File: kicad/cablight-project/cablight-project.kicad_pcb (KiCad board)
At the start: 4 copper layers, 72 x 40 mm, 62 parts, among them J3 Screw_Term_1x4_5mm, M2.5 MountingHole_2.7mm_M2.5_ISO73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, Q1 IRLB8721PBF, SW1 switch_SPDT_SLW_121586, T1 ISL85410, U1 TPD2EUSB30, U3 ESP32-S3-WROOM-1U

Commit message: further board changes
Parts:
- B1: renamed from RESET1; value Tactile -> RESET - TACTILE SMD
- B2: renamed from BOOT1; value tactile -> BOOT - TACTILE SMD
- C5: value 10uF -> 22uF
- LED1: renamed from LED-W1; value LED -> LED 0603
- LED2: renamed from LED-OK1; value LED -> LED 0603
- SW1: value switch_SPDT_SLW_121586 -> SHUNT JUMPER
- moved C4 13.8 mm to (78.3, 50.6), turned to -90 degrees
- moved R1 3.26 mm to (94.2, 46.5)
- moved R3 1.10 mm to (92.9, 70.0)
- moved R10 0.80 mm to (72.5, 44.9)
- moved M2.5 0.47 mm to (63.4, 46.5)
- moved CP4 0.45 mm to (83.8, 59.7)
- moved CP5 0.45 mm to (81.5, 59.7)
- moved CP6 0.45 mm to (79.2, 59.7)
- moved D3 0.40 mm to (113.7, 46.1)
- moved TP2 0.32 mm to (109.6, 47.1)
- moved C9 0.31 mm to (67.7, 45.8)
- moved R11 0.30 mm to (67.7, 49.9)
- moved C6 0.30 mm to (92.9, 66.3)
- moved C8 0.30 mm to (112.6, 53.6)
- moved M2.5 0.30 mm to (122.7, 72.4)
- renumbered D10 to D2, D2 to D3, J3 to J1, RCWL-1601 to J2, USBC-V1 to USBC1
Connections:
- net 3.3V renamed 3V3
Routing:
- net PG: track 41.8 -> 44.0 mm
- net 3V3: track 97.7 -> 96.2 mm
- net /VBUS: track 22.6 -> 23.3 mm
- net ECHO: vias 3 -> 1
- net GND: vias 67 -> 77
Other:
- board size 72 x 40 mm -> 72.7 x 40 mm
- board text added: "Ultrasonic LED Controller Designed by George R. Kuegler v4.0 - 2025-12-02 Haverhill, MA github.com/gkuegler"
- board text added: "move this back measure with a caliper button from pin layout"
- board text removed: "Ultrasonic Lighting Controller Designed by George R. Kuegler v4.0 - 2025-11-24 Haverhill, MA github.com/gkuegler"
- board text removed: "move this back"

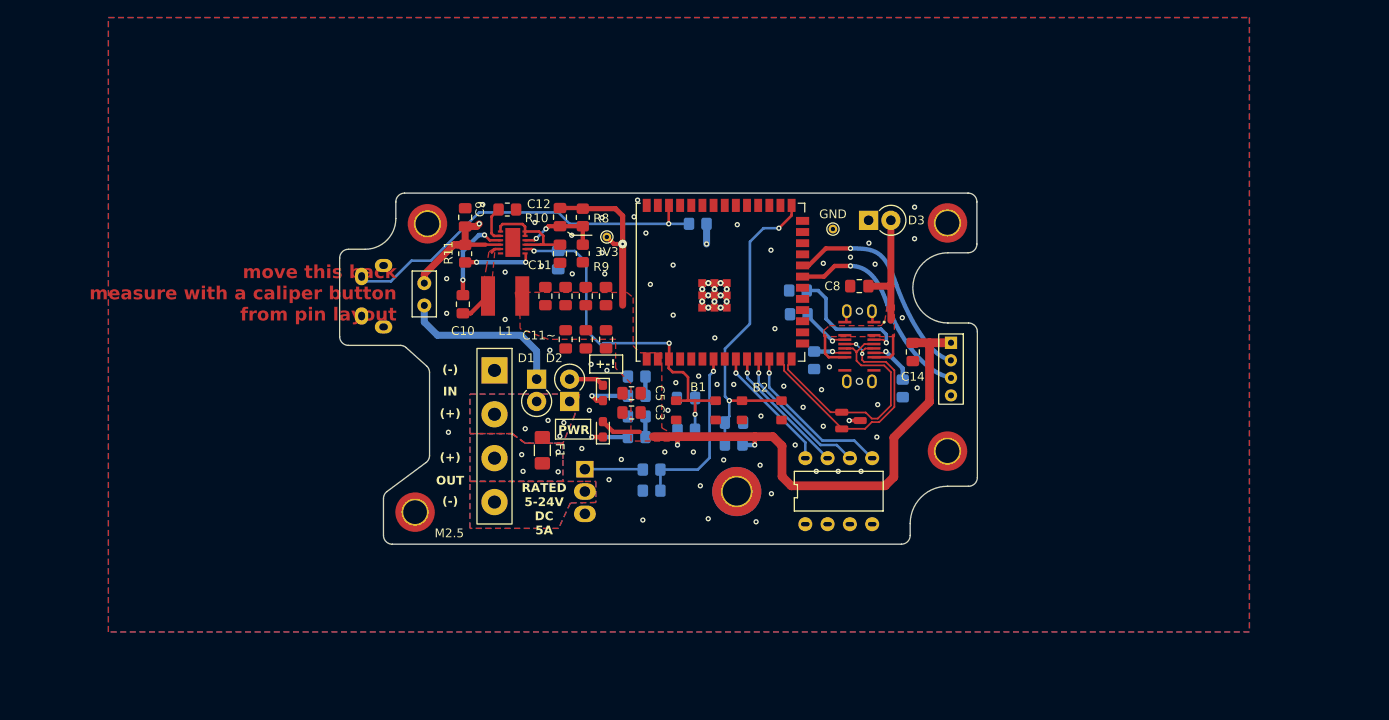
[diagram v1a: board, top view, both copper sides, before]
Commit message: add gate driver and linear regulator
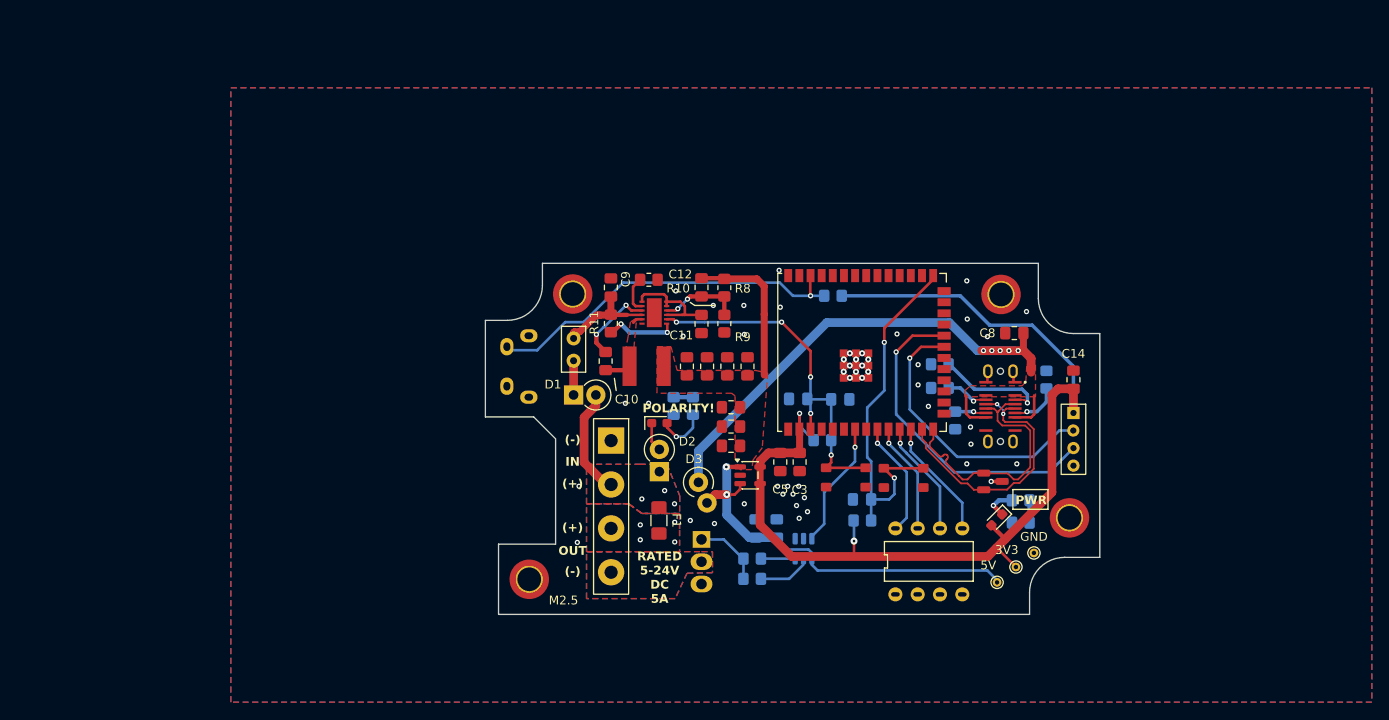
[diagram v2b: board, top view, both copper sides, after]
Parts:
- removed R4: 10K, Resistor_SMD:R_0805_2012Metric_Pad1.20x1.40mm_HandSolder
- removed REF**: MountingHole_3.2mm_M3_DIN965_Pad_TopBottom, MountingHole:MountingHole_3.2mm_M3_DIN965_Pad_TopBottom
- added C1: 2uF, Capacitor_SMD:C_0805_2012Metric_Pad1.18x1.45mm_HandSolder, B.Cu at (100.8, 81.2)
- added C2: 100nF, Capacitor_SMD:C_0805_2012Metric_Pad1.18x1.45mm_HandSolder, B.Cu at (103.2, 81.2)
- added R18: 0R, Resistor_SMD:R_0805_2012Metric_Pad1.20x1.40mm_HandSolder, B.Cu at (100.4, 84.7)
- added TP3: 5V, TestPoint:TestPoint_THTPad_D1.0mm_Drill0.5mm, F.Cu at (128.3, 87.3)
- added U2: 1EDN7550B, Package_TO_SOT_SMD:SOT-23-6, B.Cu at (106.2, 83.5)
- added U5: TLV73333PDBV, Package_TO_SOT_SMD:SOT-23-5, F.Cu at (100.2, 75.2)
- D3: value 1N5819 -> 1N5817
- R5: value 47R -> 5R
- R8: value 100K -> 91K
- R9: value 22K1 -> 12K4
- moved TP2 59.9 mm to (130.4, 85.6)
- moved LED2 46.0 mm to (128.3, 80.2), turned to -135 degrees
- moved R17 45.4 mm to (131.0, 80.5)
- moved R14 44.3 mm to (131.0, 78.0)
- moved TP1 43.4 mm to (132.5, 84.0)
- moved D3 37.1 mm to (95.2, 78.3), turned to 112.5 degrees
- moved C4 31.6 mm to (105.6, 66.5), turned to 180 degrees
- moved CP6 20.4 mm to (98.0, 67.4), turned to 180 degrees
- moved C3 20.0 mm to (105.8, 73.6), turned to -90 degrees
- moved CP5 19.3 mm to (98.0, 69.6), turned to 180 degrees
- moved B1 18.7 mm to (113.3, 76.5)
- moved CP4 18.7 mm to (98.0, 71.8), turned to 180 degrees
- moved C5 18.7 mm to (103.6, 73.6), turned to -90 degrees
- moved C14 18.6 mm to (137.0, 64.3), turned to 90 degrees
- moved C8 18.5 mm to (130.3, 59.0)
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- renumbered TP2 to TP1, TP1 to TP2
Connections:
- C12 pad 1: 3V3 -> 5V
- C9 pad 1: 5V -> Net-(SW1-B)
- CP1 pad 1: 3V3 -> 5V
- CP2 pad 1: 3V3 -> 5V
- CP3 pad 1: 3V3 -> 5V
- CP4 pad 1: 3V3 -> 5V
- CP5 pad 1: 3V3 -> 5V
- CP6 pad 1: 3V3 -> 5V
- CP7 pad 1: 3V3 -> 5V
- L1 pad 2: 3V3 -> 5V
- R11 pad 2: 5V -> Net-(SW1-B)
- R5 pad 1: LEDSIG -> Net-(U2-OUT_SRC)
- R8 pad 2: 3V3 -> 5V
- SW1 pad 2: 5V -> Net-(SW1-B)
- T1 pad 4: 5V -> Net-(SW1-B)
- U3 pad 21: ECHO -> TRIG
- U3 pad 22: TRIG -> ECHO
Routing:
- net GND: track 3.95 -> 47.7 mm, vias 77 -> 48
- net /VBUS: track 23.3 -> 65.9 mm, vias 0 -> 5
- net ECHO: track 6.08 -> 37.4 mm
- net TRIG: track 6.31 -> 32.4 mm
- net 3V3: track 96.2 -> 119.2 mm, vias 4 -> 2
- net Net-(D1-K): track 19.3 -> 3.90 mm
- net 24VDC: track 0.76 -> 13.5 mm, vias 4 -> 3
- net Net-(SW1-B): track 0.00 -> 12.3 mm
- net Net-(U2-OUT_SRC): track 0.00 -> 5.53 mm
- net LEDSIG: track 20.1 -> 14.6 mm
- net 5V: track 60.5 -> 65.8 mm, vias 1 -> 2
- net Net-(U3-GPIO0/BOOT): track 37.8 -> 43.0 mm
- net DIP3: track 18.8 -> 13.8 mm
- net Net-(U2-OUT_SNK): track 0.00 -> 3.90 mm
- net DIP2: track 16.8 -> 13.3 mm
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- added copper zone on F.Cu, net 5V
- removed copper zone on F.Cu, net 3V3
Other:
- board size 72.7 x 40 mm -> 70 x 40 mm
- board text added: "POLARITY!"
- board text added: "Ultrasonic LED Controller Designed by George R. Kuegler v4.0 2026-01-16 Haverhill, MA github.com/gkuegler"
- board text added: "_, ,_ .'/ ,_ \'. | \__( >__/ | \ / '-..__ __..-' /_\"
- board text added: "__ /\ \ / /\ \ / /__\ \ \/____\/"
- board text removed: "+-!"
- board text removed: "C11~"
- board text removed: "Ultrasonic LED Controller Designed by George R. Kuegler v4.0 - 2025-12-02 Haverhill, MA github.com/gkuegler"

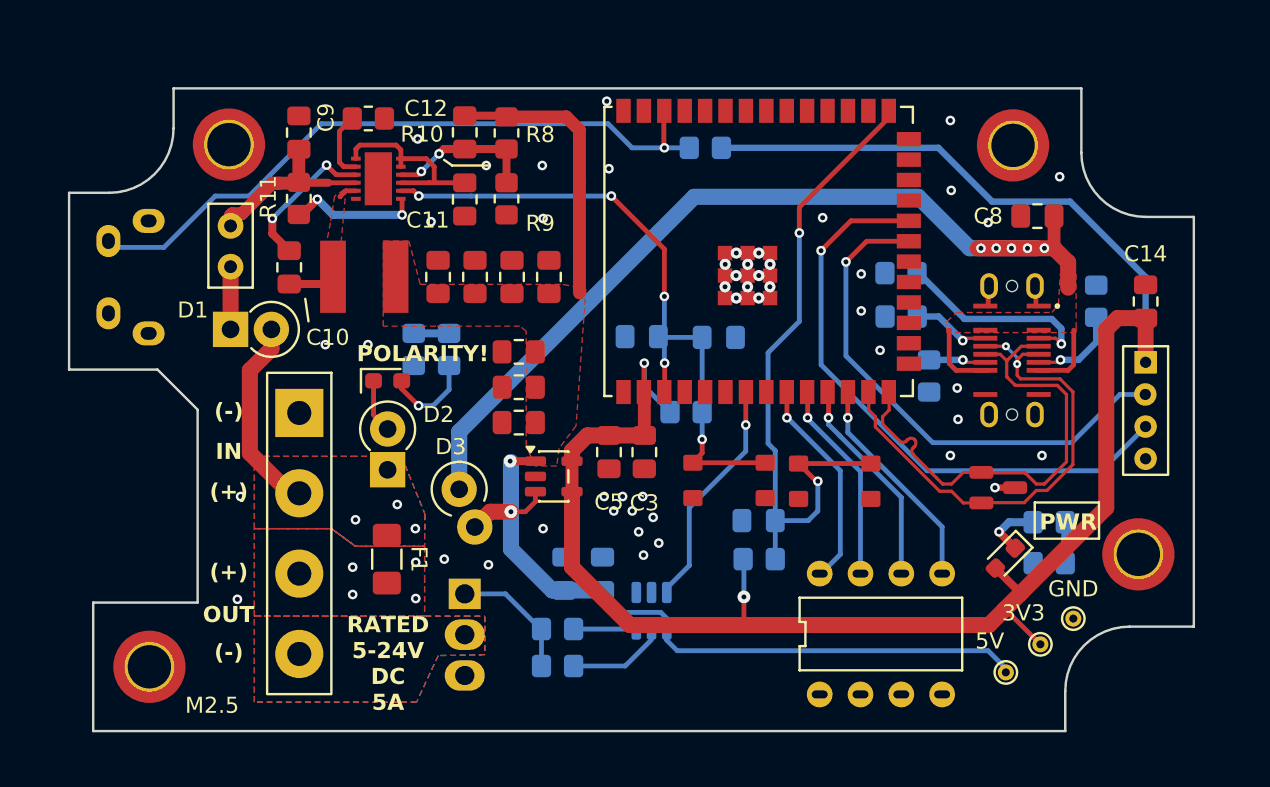
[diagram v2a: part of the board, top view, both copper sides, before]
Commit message: align button to correct location
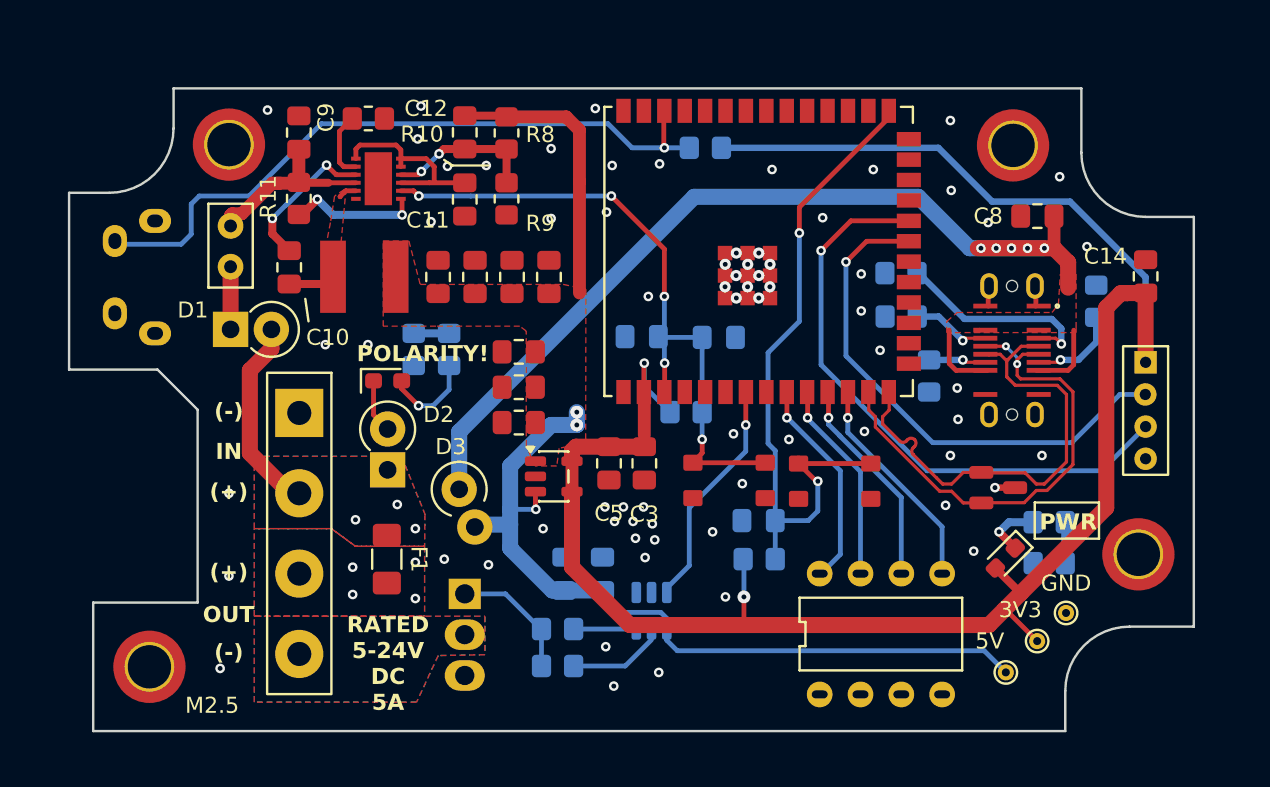
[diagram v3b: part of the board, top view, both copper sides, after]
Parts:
- moved C14 1.56 mm to (137.0, 62.7)
- moved C3 0.70 mm to (105.8, 74.3)
- moved C5 0.70 mm to (103.6, 74.3)
- moved TP1 0.57 mm to (132.1, 83.7)
- moved BTN1 0.40 mm to (72.8, 62.8)
- moved TP2 0.28 mm to (130.2, 85.4)
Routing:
- net GND: track 47.7 -> 3.95 mm, vias 48 -> 69
- net 5V: track 65.8 -> 70.0 mm, vias 2 -> 3
- net 3V3: track 119.2 -> 122.0 mm

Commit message: generate prelim output for gerbers
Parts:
- removed R18: 0R, Resistor_SMD:R_0805_2012Metric_Pad1.20x1.40mm_HandSolder
- R5: value 5R -> 10R
- moved R5 1.95 mm to (100.3, 85.0)
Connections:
- R5 pad 1: Net-(U2-OUT_SRC) -> Net-(U2-OUT_SNK)
- U2 pad 5: Net-(U2-OUT_SRC) -> Net-(U2-OUT_SNK)
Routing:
- net Net-(U2-OUT_SRC): track 5.53 -> 0.00 mm
- net 24VDC: track 13.5 -> 9.89 mm
- net /VBUS: track 66.3 -> 63.2 mm, vias 5 -> 2
- net Net-(Q1-G): track 8.00 -> 5.70 mm
- net 5V: track 70.0 -> 71.6 mm
- net Net-(U2-OUT_SNK): track 3.90 -> 4.85 mm
- net Net-(U3-GPIO0/BOOT): track 43.0 -> 43.6 mm
- net 3V3: track 122.0 -> 122.5 mm
- net GND: vias 69 -> 68

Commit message: jlpcb order
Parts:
- added G***: LOGO, Library:logo_12, F.Cu at (108.2, 86.3)
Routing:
- net GND: vias 68 -> 69
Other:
- outline, holes or cut-outs redrawn
